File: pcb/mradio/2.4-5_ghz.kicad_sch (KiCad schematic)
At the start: 21 parts, among them J501 MDT420E01001

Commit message: Fixed passive numbers
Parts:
- renumbered C504 to C502, C502 to C503, C505 to C504, R508 to R501, R509 to R502, R501 to R503, R502 to R504, R504 to R508
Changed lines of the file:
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@@
 		(dnp no)
 		(fields_autoplaced yes)
-		(property "Reference" "#PWR0515"
+		(property "Reference" "#PWR0501"
 			(at 57.15 87.63 0)
 			(hide yes)
@@
 			(project "mradio"
 				(path "/a3cfb3f7-0a76-4383-aac7-b46c1ac4283d"
-					(reference "#PWR0515")
+					(reference "#PWR0501")
 					(unit 1)
 				)
@@
 		(dnp no)
 		(fields_autoplaced yes)
-		(property "Reference" "#PWR0525"
+		(property "Reference" "#PWR0529"
 			(at 193.04 120.65 0)
 			(hide yes)
@@
 			(project "mradio"
 				(path "/a3cfb3f7-0a76-4383-aac7-b46c1ac4283d"
-					(reference "#PWR0525")
+					(reference "#PWR0529")
 					(unit 1)
 				)
@@
 		(dnp no)
 		(fields_autoplaced yes)
-		(property "Reference" "#PWR0519"
+		(property "Reference" "#PWR0536"
 			(at 207.01 92.71 0)
 			(hide yes)
@@
 			(project "mradio"
 				(path "/a3cfb3f7-0a76-4383-aac7-b46c1ac4283d"
-					(reference "#PWR0519")
+					(reference "#PWR0536")
 					(unit 1)
 				)
@@
 		(dnp no)
 		(fields_autoplaced yes)
-		(property "Reference" "R509"
+		(property "Reference" "R502"
 			(at 104.14 123.19 90)
 			(show_name no)
@@
 			(project "mradio"
 				(path "/a3cfb3f7-0a76-4383-aac7-b46c1ac4283d"
-					(reference "R509")
+					(reference "R502")
 					(unit 1)
 				)
@@
 		(dnp no)
 		(fields_autoplaced yes)
-		(property "Reference" "#PWR0508"
+		(property "Reference" "#PWR0514"
 			(at 149.86 77.47 0)
 			(hide yes)
@@
 			(project "mradio"
 				(path "/a3cfb3f7-0a76-4383-aac7-b46c1ac4283d"
-					(reference "#PWR0508")
+					(reference "#PWR0514")
 					(unit 1)
 				)
@@
 		(dnp no)
 		(fields_autoplaced yes)
-		(property "Reference" "R504"
+		(property "Reference" "R508"
 			(at 200.66 31.7499 0)
 			(show_name no)
@@
 			(project "mradio"
 				(path "/a3cfb3f7-0a76-4383-aac7-b46c1ac4283d"
-					(reference "R504")
+					(reference "R508")
 					(unit 1)
 				)
@@
 		(dnp no)
 		(fields_autoplaced yes)
-		(property "Reference" "#PWR0506"
+		(property "Reference" "#PWR0513"
 			(at 149.86 69.85 0)
 			(hide yes)
@@
 			(project "mradio"
 				(path "/a3cfb3f7-0a76-4383-aac7-b46c1ac4283d"
-					(reference "#PWR0506")
+					(reference "#PWR0513")
 					(unit 1)
 				)
@@
 		(dnp no)
 		(fields_autoplaced yes)
-		(property "Reference" "C504"
+		(property "Reference" "C502"
 			(at 118.11 142.2399 0)
 			(show_name no)
@@
 			(project "mradio"
 				(path "/a3cfb3f7-0a76-4383-aac7-b46c1ac4283d"
-					(reference "C504")
+					(reference "C502")
 					(unit 1)
 				)
@@
 		(dnp no)
 		(fields_autoplaced yes)
-		(property "Reference" "#PWR0528"
+		(property "Reference" "#PWR0503"
 			(at 104.14 129.54 0)
 			(hide yes)
@@
 			(project "mradio"
 				(path "/a3cfb3f7-0a76-4383-aac7-b46c1ac4283d"
-					(reference "#PWR0528")
+					(reference "#PWR0503")
 					(unit 1)
 				)
@@
 		(dnp no)
 		(fields_autoplaced yes)
-		(property "Reference" "#PWR0535"
+		(property "Reference" "#PWR0524"
 			(at 179.07 157.48 0)
 			(hide yes)
@@
 			(project "mradio"
 				(path "/a3cfb3f7-0a76-4383-aac7-b46c1ac4283d"
-					(reference "#PWR0535")
+					(reference "#PWR0524")
 					(unit 1)
 				)
@@
 		(dnp no)
 		(fields_autoplaced yes)
-		(property "Reference" "#PWR0526"
+		(property "Reference" "#PWR0502"
 			(at 100.33 119.38 0)
 			(hide yes)
@@
 			(project "mradio"
 				(path "/a3cfb3f7-0a76-4383-aac7-b46c1ac4283d"
-					(reference "#PWR0526")
+					(reference "#PWR0502")
 					(unit 1)
 				)
@@
 		(dnp no)
 		(fields_autoplaced yes)
-		(property "Reference" "C502"
+		(property "Reference" "C503"
 			(at 180.34 92.7099 0)
 			(show_name no)
@@
 			(project "mradio"
 				(path "/a3cfb3f7-0a76-4383-aac7-b46c1ac4283d"
-					(reference "C502")
+					(reference "C503")
 					(unit 1)
 				)
@@
 		(dnp no)
 		(fields_autoplaced yes)
-		(property "Reference" "R508"
+		(property "Reference" "R501"
 			(at 100.33 113.03 90)
 			(show_name no)
@@
 			(project "mradio"
 				(path "/a3cfb3f7-0a76-4383-aac7-b46c1ac4283d"
-					(reference "R508")
+					(reference "R501")
 					(unit 1)
 				)
@@
 		(dnp no)
 		(fields_autoplaced yes)
-		(property "Reference" "R501"
+		(property "Reference" "R503"
 			(at 173.99 31.7499 0)
 			(show_name no)
@@
 			(project "mradio"
 				(path "/a3cfb3f7-0a76-4383-aac7-b46c1ac4283d"
-					(reference "R501")
+					(reference "R503")
 					(unit 1)
 				)
@@
 		(in_pos_files yes)
 		(dnp no)
-		(property "Reference" "#PWR0522"
+		(property "Reference" "#PWR0527"
 			(at 191.77 106.68 0)
 			(hide yes)
@@
 			(project "mradio"
 				(path "/a3cfb3f7-0a76-4383-aac7-b46c1ac4283d"
-					(reference "#PWR0522")
+					(reference "#PWR0527")
 					(unit 1)
 				)
@@
 		(dnp no)
 		(fields_autoplaced yes)
-		(property "Reference" "#PWR0534"
+		(property "Reference" "#PWR0507"
 			(at 114.3 153.67 0)
 			(hide yes)
@@
 			(project "mradio"
 				(path "/a3cfb3f7-0a76-4383-aac7-b46c1ac4283d"
-					(reference "#PWR0534")
+					(reference "#PWR0507")
 					(unit 1)
 				)
@@
 		(dnp no)
 		(fields_autoplaced yes)
-		(property "Reference" "#PWR0509"
+		(property "Reference" "#PWR0534"
 			(at 207.01 74.93 0)
 			(hide yes)
@@
 			(project "mradio"
 				(path "/a3cfb3f7-0a76-4383-aac7-b46c1ac4283d"
-					(reference "#PWR0509")
+					(reference "#PWR0534")
 					(unit 1)
 				)
@@
 		(dnp no)
 		(fields_autoplaced yes)
-		(property "Reference" "#PWR0521"
+		(property "Reference" "#PWR0522"
 			(at 176.53 104.14 0)
 			(hide yes)
@@
 			(project "mradio"
 				(path "/a3cfb3f7-0a76-4383-aac7-b46c1ac4283d"
-					(reference "#PWR0521")
+					(reference "#PWR0522")
 					(unit 1)
 				)
@@
 		(dnp no)
 		(fields_autoplaced yes)
-		(property "Reference" "#PWR0536"
+		(property "Reference" "#PWR0531"
 			(at 195.58 160.02 0)
 			(hide yes)
@@
 			(project "mradio"
 				(path "/a3cfb3f7-0a76-4383-aac7-b46c1ac4283d"
-					(reference "#PWR0536")
+					(reference "#PWR0531")
 					(unit 1)
 				)
@@
 		(dnp no)
 		(fields_autoplaced yes)
-		(property "Reference" "#PWR0529"
+		(property "Reference" "#PWR0532"
 			(at 190.5 130.81 0)
 			(hide yes)
@@
 			(project "mradio"
 				(path "/a3cfb3f7-0a76-4383-aac7-b46c1ac4283d"
-					(reference "#PWR0529")
+					(reference "#PWR0532")
 					(unit 1)
 				)
@@
 		(dnp no)
 		(fields_autoplaced yes)
-		(property "Reference" "#PWR0512"
+		(property "Reference" "#PWR0535"
 			(at 217.17 77.47 0)
 			(hide yes)
@@
 			(project "mradio"
 				(path "/a3cfb3f7-0a76-4383-aac7-b46c1ac4283d"
-					(reference "#PWR0512")
+					(reference "#PWR0535")
 					(unit 1)
 				)
@@
 		(dnp no)
 		(fields_autoplaced yes)
-		(property "Reference" "#PWR0511"
+		(property "Reference" "#PWR0528"
 			(at 186.69 77.47 0)
 			(hide yes)
@@
 			(project "mradio"
 				(path "/a3cfb3f7-0a76-4383-aac7-b46c1ac4283d"
-					(reference "#PWR0511")
+					(reference "#PWR0528")
 					(unit 1)
 				)
@@
 		(dnp no)
 		(fields_autoplaced yes)
-		(property "Reference" "R502"
+		(property "Reference" "R504"
 			(at 182.88 31.7499 0)
 			(show_name no)
@@
 			(project "mradio"
 				(path "/a3cfb3f7-0a76-4383-aac7-b46c1ac4283d"
-					(reference "R502")
+					(reference "R504")
 					(unit 1)
 				)
@@
 		(dnp no)
 		(fields_autoplaced yes)
-		(property "Reference" "C505"
+		(property "Reference" "C504"
 			(at 182.88 146.0499 0)
 			(show_name no)
@@
 			(project "mradio"
 				(path "/a3cfb3f7-0a76-4383-aac7-b46c1ac4283d"
-					(reference "C505")
+					(reference "C504")
 					(unit 1)
 				)
@@
 		(dnp no)
 		(fields_autoplaced yes)
-		(property "Reference" "#PWR0514"
+		(property "Reference" "#PWR0515"
 			(at 149.86 85.09 0)
 			(hide yes)
@@
 			(project "mradio"
 				(path "/a3cfb3f7-0a76-4383-aac7-b46c1ac4283d"
-					(reference "#PWR0514")
-					(unit 1)
-				)
+					(reference "#PWR0515")
+					(unit 1)
+				)

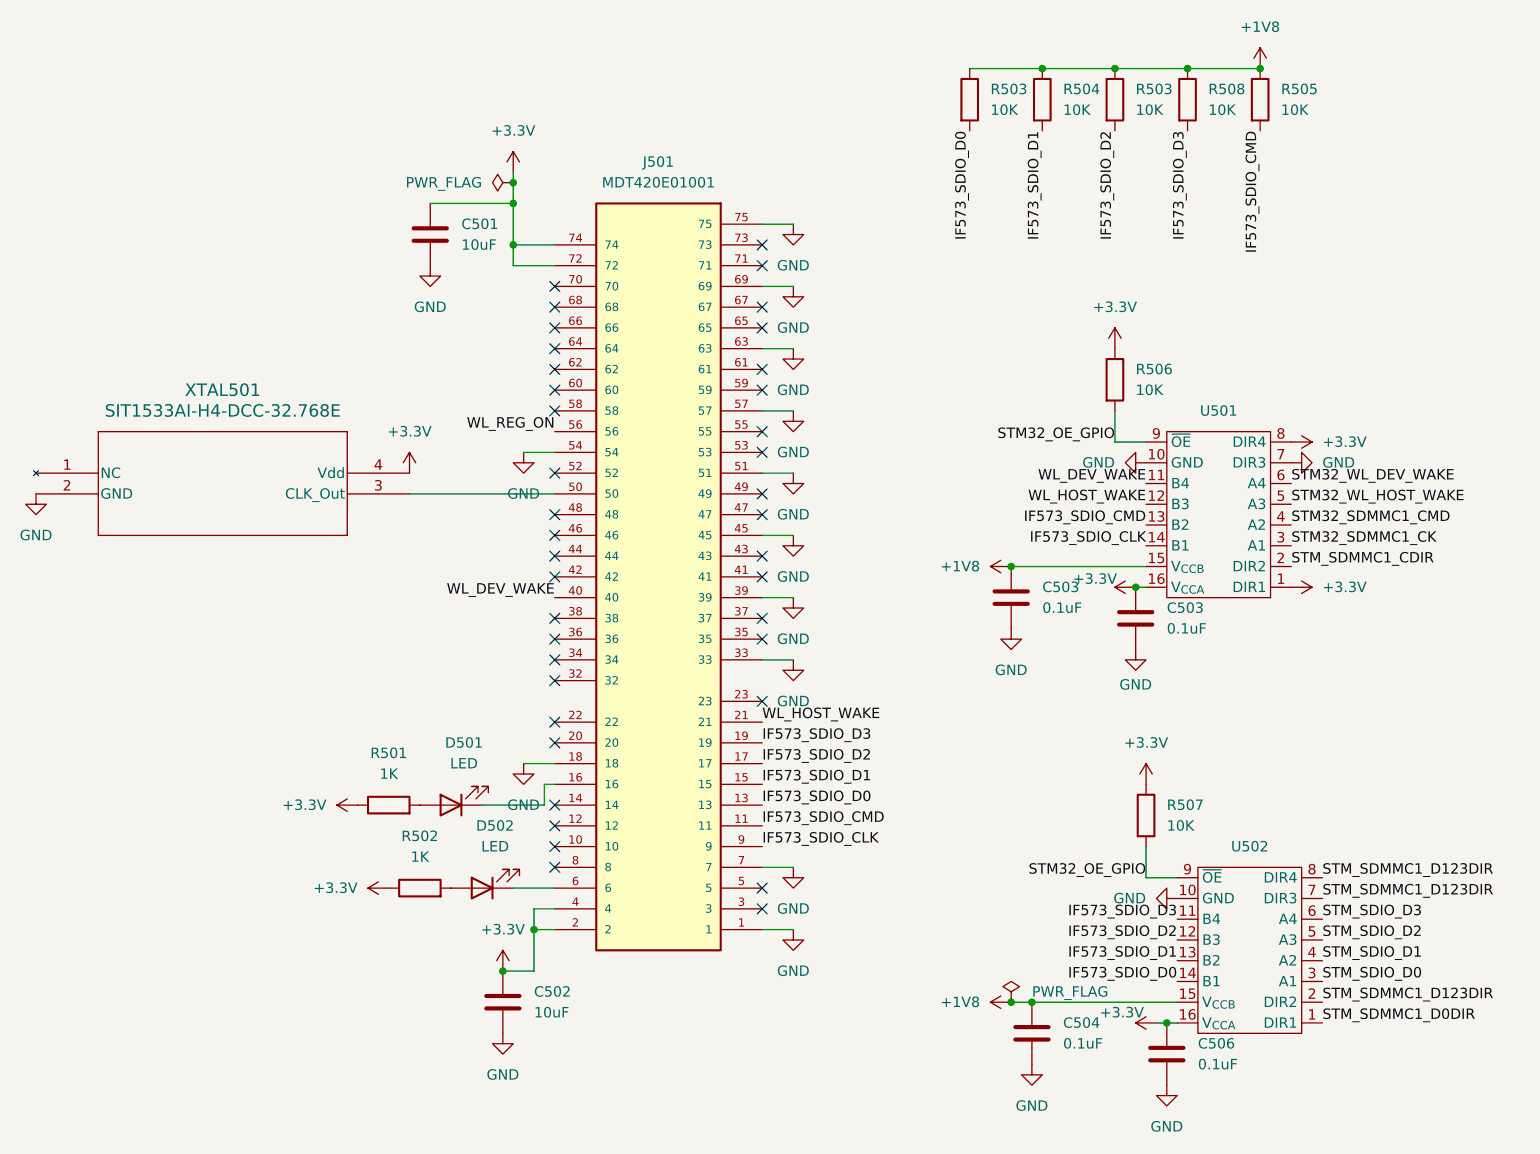
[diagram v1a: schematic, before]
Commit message: update wifi and add global labels
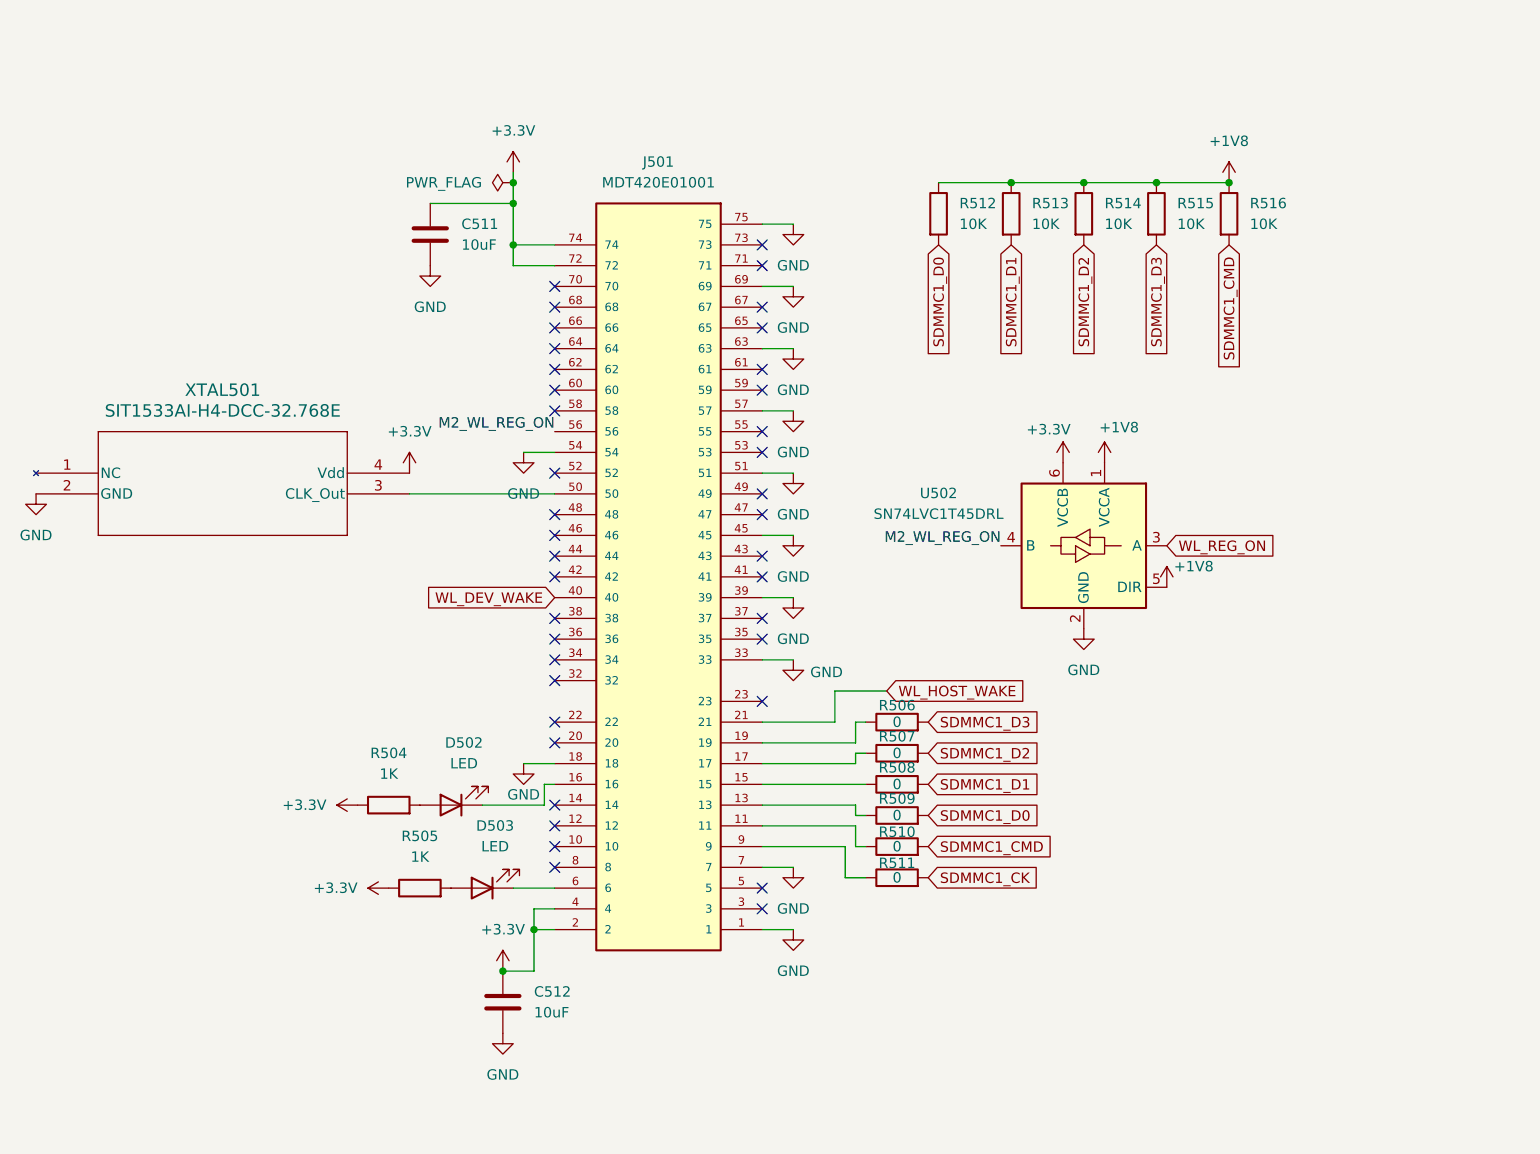
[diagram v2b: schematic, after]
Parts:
- removed C503 (x2), C504, C506: 0.1uF, Capacitor_SMD:C_0603_1608Metric, symbol Device:C
- removed U501, U502: (no value), Package_SO:TSSOP-16_4.4x5mm_P0.65mm, symbol 74AVC4T774QPWRQ1:74AVC4T774QPWRQ1
- added R508, R509, R510, R511: 0, symbol Device:R
- added U502: SN74LVC1T45DRL, Package_TO_SOT_SMD:SOT-563, symbol Logic_LevelTranslator:SN74LVC1T45DRL
- R506, R507: value 10K -> 0; footprint Resistor_SMD:R_0603_1608Metric -> (none)
- renumbered C501 to C511, C502 to C512, D501 to D502, D502 to D503, R501 to R504, R502 to R505, R503 to R512, R504 to R513, R503 to R514, R508 to R515, R505 to R516
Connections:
- net +1V8: now also U502.1 (VCCA), U502.5 (DIR)
- net +3.3V: now also U502.6 (VCCB); no longer R506.1, R507.1
- net GND: now also U502.2 (GND)
- net WL_REG_ON: now also U502.3 (A); no longer J501.56
- net IF573_SDIO_CLK: no longer names the net of J501.9
- net IF573_SDIO_CLK: now also R511.1
- net IF573_SDIO_CMD: no longer names the net of J501.11
- net IF573_SDIO_CMD: now also R510.1; no longer R516.2
- net IF573_SDIO_D0: no longer names the net of J501.13
- net IF573_SDIO_D0: now also R509.1; no longer R512.2
- net IF573_SDIO_D1: no longer names the net of J501.15
- net IF573_SDIO_D1: now also R508.1; no longer R513.2
- net IF573_SDIO_D2: no longer names the net of J501.17
- net IF573_SDIO_D2: now also R507.1; no longer R514.2
- net IF573_SDIO_D3: no longer names the net of J501.19
- net IF573_SDIO_D3: now also R506.1; no longer R515.2
- net STM32_OE_GPIO renamed SDMMC1_D2
- net SDMMC1_D2: now also R514.2; no longer R506.2
- new net M2_WL_REG_ON: J501.56, U502.4 (B)
- new net SDMMC1_CK: R511.2
- new net SDMMC1_CMD: R510.2, R516.2
- new net SDMMC1_D0: R509.2, R512.2
- new net SDMMC1_D1: R508.2, R513.2
- new net SDMMC1_D3: R506.2, R515.2
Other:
- moved on the sheet: R512, R513, R514, R515, R516

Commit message: Schematic review updates
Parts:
- removed R508, R509, R510, R511: 0, symbol Device:R
- removed U502: SN74LVC1T45DRL, Package_TO_SOT_SMD:SOT-563, symbol Logic_LevelTranslator:SN74LVC1T45DRL
- added C503, C504, C505, C506: 0.1uF, Capacitor_SMD:C_0603_1608Metric, symbol Device:C
- added U501, U502: (no value), Package_SO:TSSOP-16_4.4x5mm_P0.65mm, symbol 74AVC4T774QPWRQ1:74AVC4T774QPWRQ1
- R506, R507: value 0 -> 10K; footprint (none) -> Resistor_SMD:R_0603_1608Metric
- renumbered C511 to C501, C512 to C502, D502 to D501, D503 to D502, R504 to R501, R505 to R502, R512 to R503, R513 to R504, R514 to R505, R515 to R508, R516 to R509
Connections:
- net M2_WL_REG_ON is gone; now on net WL_REG_ON: J501.56
- net SDMMC1_CMD is gone; now on net IF573_SDIO_CMD: R509.2
- net SDMMC1_D0 is gone; now on net IF573_SDIO_D0: R503.2
- net SDMMC1_D1 is gone; now on net IF573_SDIO_D1: R504.2
- net +1V8: now also C503.1, C504.1, U501.15 (V_{CCB}), U502.15 (V_{CCB})
- net +3.3V: now also R506.1, R507.1, C505.1, C506.1, U501.1 (DIR1), U501.16 (V_{CCA}), U501.8 (DIR4), U502.16 (V_{CCA})
- net GND: now also C503.2, C504.2, C505.2, C506.2, U501.10 (GND), U501.7 (DIR3), U502.10 (GND)
- net WL_DEV_WAKE: now also U501.11 (B4)
- net WL_HOST_WAKE: now also U501.12 (B3)
- net IF573_SDIO_D0: now reaches J501.13
- net IF573_SDIO_D0: now also U502.14 (B1)
- net IF573_SDIO_D3: now reaches J501.19
- net IF573_SDIO_D3: now also R508.2, U502.11 (B4); no longer R506.1
- net IF573_SDIO_CMD: now reaches J501.11
- net IF573_SDIO_CMD: now also U501.13 (B2)
- net IF573_SDIO_D1: now reaches J501.15
- net IF573_SDIO_D1: now also U502.13 (B2)
- net IF573_SDIO_D2: now reaches J501.17
- net IF573_SDIO_D2: now also R505.2, U502.12 (B3); no longer R507.1
- net IF573_SDIO_CLK: now reaches J501.9
- net IF573_SDIO_CLK: now also U501.14 (B1)
- net SDMMC1_D2 renamed STM32_OE_GPIO
- net STM32_OE_GPIO: now also R506.2, U501.9 (~{OE}), U502.9 (~{OE}); no longer R505.2
- removed net SDMMC1_D3: R506.2, R508.2
- new net STM32_SDMMC1_CK: U501.3 (A1)
- new net STM32_SDMMC1_CMD: U501.4 (A2)
- new net STM32_WL_DEV_WAKE: U501.6 (A4)
- new net STM32_WL_HOST_WAKE: U501.5 (A3)
- new net STM_SDIO_D0: U502.3 (A1)
- new net STM_SDIO_D1: U502.4 (A2)
- new net STM_SDIO_D2: U502.5 (A3)
- new net STM_SDIO_D3: U502.6 (A4)
- new net STM_SDMMC1_CDIR: U501.2 (DIR2)
- new net STM_SDMMC1_D0DIR: U502.1 (DIR1)
- new net STM_SDMMC1_D123DIR: U502.2 (DIR2), U502.7 (DIR3), U502.8 (DIR4)
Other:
- moved on the sheet: R503, R504, R505, R508, R509

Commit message: undid overwrite
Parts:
- removed C503, C504, C505, C506: 0.1uF, Capacitor_SMD:C_0603_1608Metric, symbol Device:C
- removed U501, U502: (no value), Package_SO:TSSOP-16_4.4x5mm_P0.65mm, symbol 74AVC4T774QPWRQ1:74AVC4T774QPWRQ1
- added R508, R509, R510, R511: 0, symbol Device:R
- added U502: SN74LVC1T45DRL, Package_TO_SOT_SMD:SOT-563, symbol Logic_LevelTranslator:SN74LVC1T45DRL
- R506, R507: value 10K -> 0; footprint Resistor_SMD:R_0603_1608Metric -> (none)
- renumbered C501 to C511, C502 to C512, D501 to D502, D502 to D503, R501 to R504, R502 to R505, R503 to R512, R504 to R513, R505 to R514, R508 to R515, R509 to R516
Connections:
- net +1V8: now also U502.1 (VCCA), U502.5 (DIR)
- net +3.3V: now also U502.6 (VCCB); no longer R506.1, R507.1
- net GND: now also U502.2 (GND)
- net WL_REG_ON: now also U502.3 (A); no longer J501.56
- net IF573_SDIO_CLK: no longer names the net of J501.9
- net IF573_SDIO_CLK: now also R511.1
- net IF573_SDIO_CMD: no longer names the net of J501.11
- net IF573_SDIO_CMD: now also R510.1; no longer R516.2
- net IF573_SDIO_D0: no longer names the net of J501.13
- net IF573_SDIO_D0: now also R509.1; no longer R512.2
- net IF573_SDIO_D1: no longer names the net of J501.15
- net IF573_SDIO_D1: now also R508.1; no longer R513.2
- net IF573_SDIO_D2: no longer names the net of J501.17
- net IF573_SDIO_D2: now also R507.1; no longer R514.2
- net IF573_SDIO_D3: no longer names the net of J501.19
- net IF573_SDIO_D3: now also R506.1; no longer R515.2
- net STM32_OE_GPIO renamed SDMMC1_D2
- net SDMMC1_D2: now also R514.2; no longer R506.2
- new net M2_WL_REG_ON: J501.56, U502.4 (B)
- new net SDMMC1_CK: R511.2
- new net SDMMC1_CMD: R510.2, R516.2
- new net SDMMC1_D0: R509.2, R512.2
- new net SDMMC1_D1: R508.2, R513.2
- new net SDMMC1_D3: R506.2, R515.2
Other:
- moved on the sheet: R512, R513, R514, R515, R516
